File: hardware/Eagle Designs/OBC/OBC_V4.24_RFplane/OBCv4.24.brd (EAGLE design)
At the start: 90.2 x 95.5 mm, 38 parts, among them J1 MCX-J-P-H-RA-TH1, J10 5037630591, J11 5037630291, J12 5037630491, J13 5037630291, J14 5037630491, J2 5037630491, J3 5037630591, J4 5037630291, J5 5037630291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

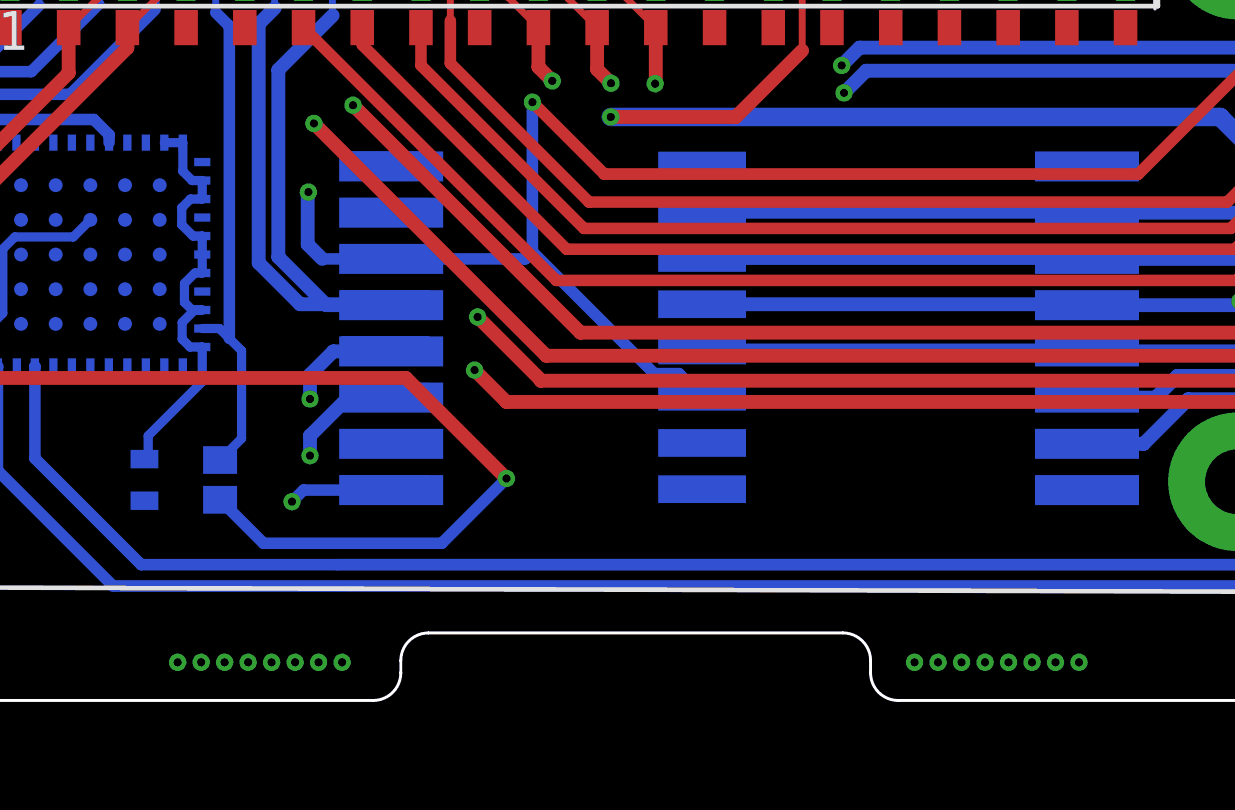
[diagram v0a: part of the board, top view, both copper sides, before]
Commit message: Added RF plane to OBCv4.24
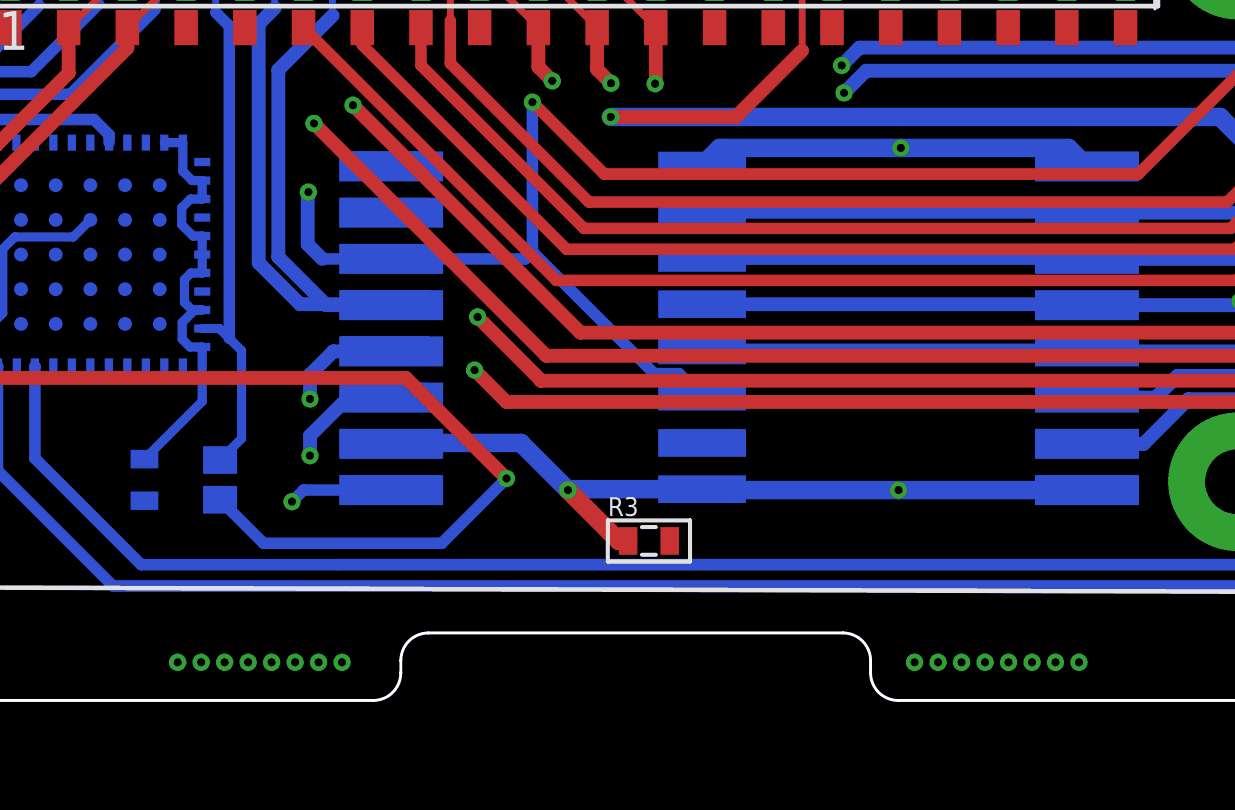
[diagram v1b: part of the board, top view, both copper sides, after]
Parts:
- added R3: 1M, HSFL_Main_Library:0805
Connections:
- new net GPS_GND: R6.1, U6.21, U6.22, U6.24, U6.25, U6.27, U6.28, U6.29, U6.31, U6.33
- net GND: now also R3.2; no longer J1.S1, J1.S2, J1.S3, J1.S4, U3.1, U3.10, U3.8, U4.1, U4.10, U4.8
- net RF_GND: now also J1.S1, J1.S2, J1.S3, J1.S4, R3.1, U3.1, U3.10, U3.8, U4.1, U4.10, U4.8; no longer R6.1, U6.21, U6.22, U6.24, U6.25, U6.27, U6.28, U6.29, U6.31, U6.33
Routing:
- net RF_GND: track 19.8 -> 52.3 mm, vias 0 -> 3
- net GPS_GND: track 0.00 -> 19.8 mm
- added copper zone on layer 15, net RF_GND
